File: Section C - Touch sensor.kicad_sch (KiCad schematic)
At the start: 5 parts, among them U2 AT42QT1012-T

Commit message: touch pad library creation
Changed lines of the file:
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@@
 	(rectangle
 		(start 60.96 48.26)
-		(end 229.87 148.59)
+		(end 185.42 148.59)
 		(stroke
 			(width 1)
@@
 	(text_box "DESIGN NOTE:\nblabla"
 		(exclude_from_sim no)
-		(at 127 129.54 0)
+		(at 119.38 124.46 0)
 		(size 21.59 15.24)
 		(margins 1.3525 1.3525 1.3525 1.3525)
@@
 	(text_box "LAYOUT NOTE:\nblabla"
 		(exclude_from_sim no)
-		(at 180.34 63.5 0)
+		(at 91.44 124.46 0)
 		(size 26.67 15.24)
 		(margins 1.4525 1.4525 1.4525 1.4525)
@@
 		(exclude_from_sim no)
 		(at 160.02 111.76 0)
-		(size 21.59 11.43)
+		(size 20.32 11.43)
 		(margins 1.3525 1.3525 1.3525 1.3525)
 		(stroke

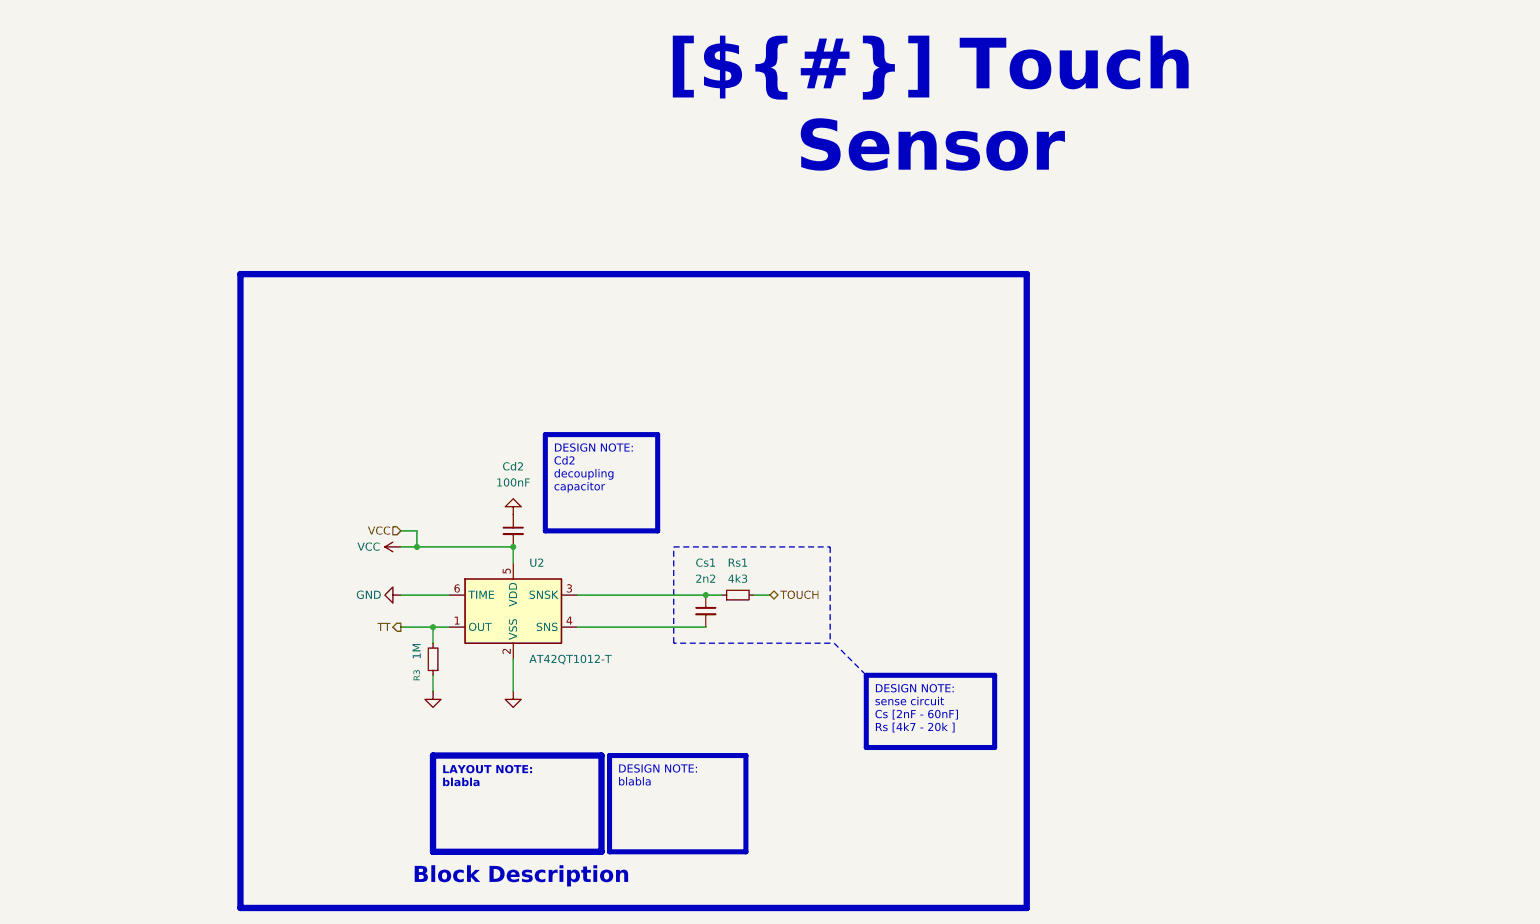
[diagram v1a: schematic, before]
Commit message: [sch] update touch sensor section
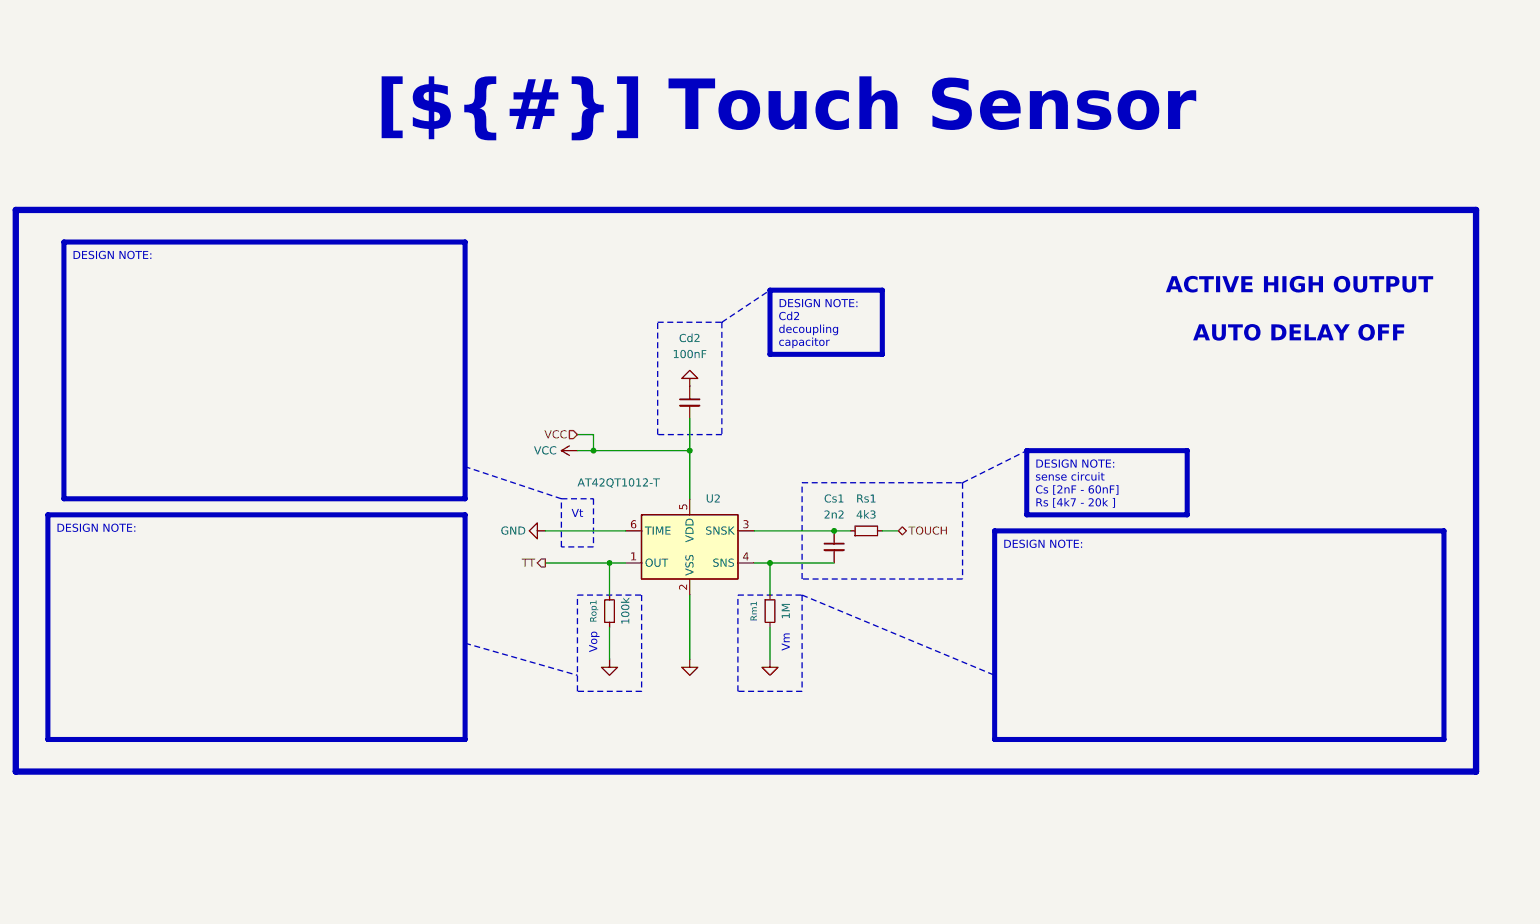
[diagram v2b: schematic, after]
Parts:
- added Rm1: 1M, Resistor_SMD:R_0805_2012Metric, symbol Device:R_Small
- Rop1: renamed from R3; value 1M -> 100k
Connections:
- net GND: now also Rm1.2
- net at Cs1.2, U2.4 (SNS): now also Rm1.1
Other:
- note added: "Vm"
- note added: "Vop"
- note added: "Vt"
- moved on the sheet: Cd2, Cs1, Rop1, Rs1, U2

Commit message: [CFG] Configuration update, added bom information fields
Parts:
- U2: BOM_INFO (none) -> TME have; BOM_STATUS (none) -> OK

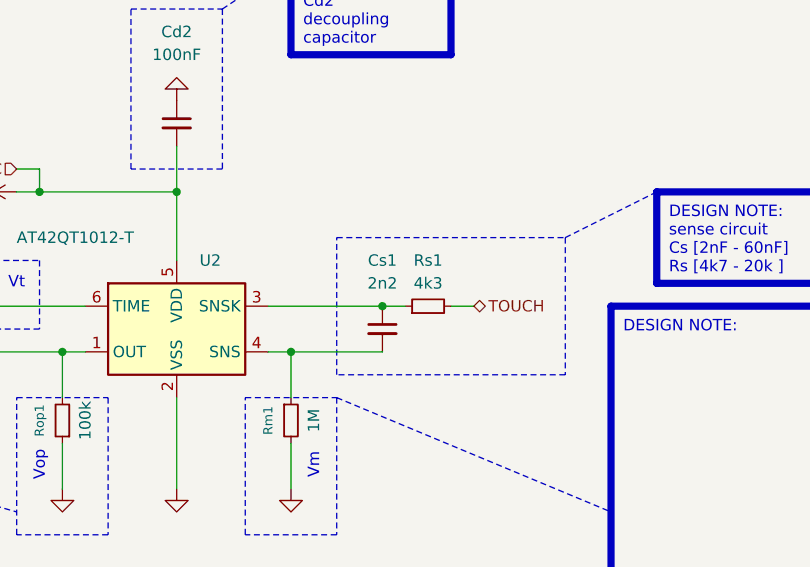
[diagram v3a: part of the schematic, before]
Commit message: bom update, qr-code added
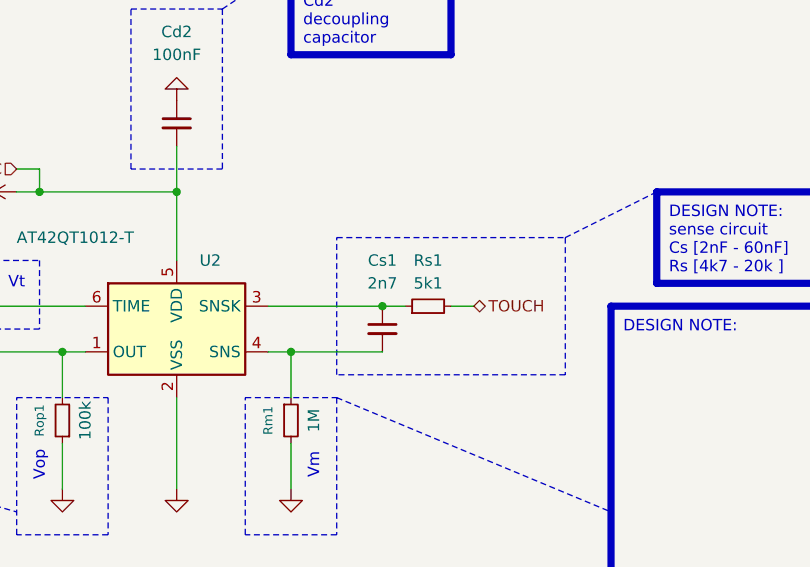
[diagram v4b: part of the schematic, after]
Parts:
- Cd2: BOM_INFO (none) -> AIDATEK A0; BOM_STATUS (none) -> OK
- Cs1: value 2n2 -> 2n7; BOM_INFO (none) -> TME BOX; BOM_STATUS (none) -> OK
- Rm1, Rop1: BOM_INFO (none) -> TME BOX; BOM_STATUS (none) -> OK
- Rs1: value 4k3 -> 5k1; BOM_INFO (none) -> TME BOX 25.06.2025; BOM_STATUS (none) -> OK
- U2: BOM_INFO TME have -> TME BOX
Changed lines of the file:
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@@
 			)
 		)
-		(property "BOM_INFO" "TME have"
+		(property "BOM_INFO" "TME BOX"
 			(at 132.08 91.44 0)
 			(effects
@@
 			)
 		)
-		(property "Value" "4k3"
+		(property "Value" "5k1"
 			(at 160.02 86.36 90)
 			(effects
@@
 			)
 		)
-		(property "BOM_INFO" ""
+		(property "BOM_INFO" "TME BOX 25.06.2025"
 			(at 160.02 88.9 90)
 			(effects
@@
 			)
 		)
-		(property "BOM_STATUS" ""
+		(property "BOM_STATUS" "OK"
 			(at 160.02 88.9 90)
 			(effects
@@
 			)
 		)
-		(property "BOM_INFO" ""
+		(property "BOM_INFO" "TME BOX "
 			(at 119.38 101.6 90)
 			(effects
@@
 			)
 		)
-		(property "BOM_STATUS" ""
+		(property "BOM_STATUS" "OK"
 			(at 119.38 101.6 90)
 			(effects
@@
 			)
 		)
-		(property "BOM_INFO" ""
+		(property "BOM_INFO" "TME BOX"
 			(at 144.78 101.6 90)
 			(effects
@@
 			)
 		)
-		(property "BOM_STATUS" ""
+		(property "BOM_STATUS" "OK"
 			(at 144.78 101.6 90)
 			(effects
@@
 			)
 		)
-		(property "BOM_INFO" ""
-			(at 132.08 68.58 0)
-			(effects
-				(font
-					(size 1.27 1.27)
-				)
-				(hide yes)
-			)
-		)
-		(property "BOM_STATUS" ""
+		(property "BOM_INFO" "AIDATEK A0"
+			(at 132.08 68.58 0)
+			(effects
+				(font
+					(size 1.27 1.27)
+				)
+				(hide yes)
+			)
+		)
+		(property "BOM_STATUS" "OK"
 			(at 132.08 68.58 0)
 			(effects
@@
 			)
 		)
-		(property "Value" "2n2"
+		(property "Value" "2n7"
 			(at 154.94 86.36 0)
 			(effects
@@
 			)
 		)
-		(property "BOM_INFO" ""
+		(property "BOM_INFO" "TME BOX"
 			(at 154.94 91.44 0)
 			(effects
@@
 			)
 		)
-		(property "BOM_STATUS" ""
+		(property "BOM_STATUS" "OK"
 			(at 154.94 91.44 0)
 			(effects

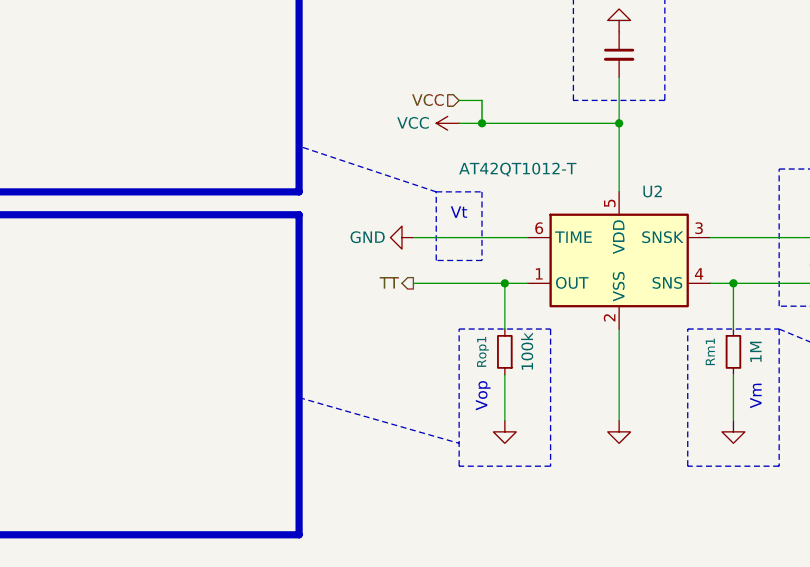
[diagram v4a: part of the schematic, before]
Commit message: [sch] added R3 to prevent high current drain from cap touch chip
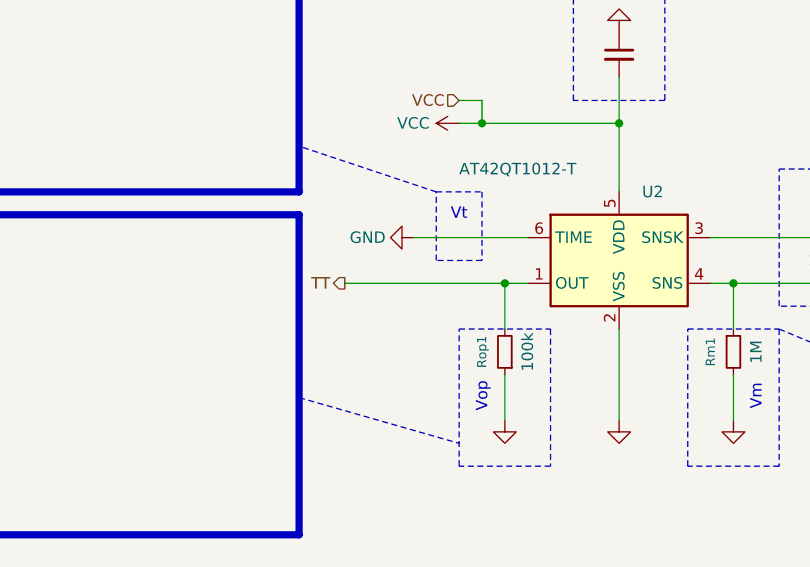
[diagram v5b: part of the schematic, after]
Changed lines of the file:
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@@
 	(wire
 		(pts
-			(xy 109.22 93.98) (xy 119.38 93.98)
+			(xy 101.6 93.98) (xy 119.38 93.98)
 		)
 		(stroke
@@
 	(hierarchical_label "TT"
 		(shape output)
-		(at 109.22 93.98 180)
+		(at 101.6 93.98 180)
 		(effects
 			(font

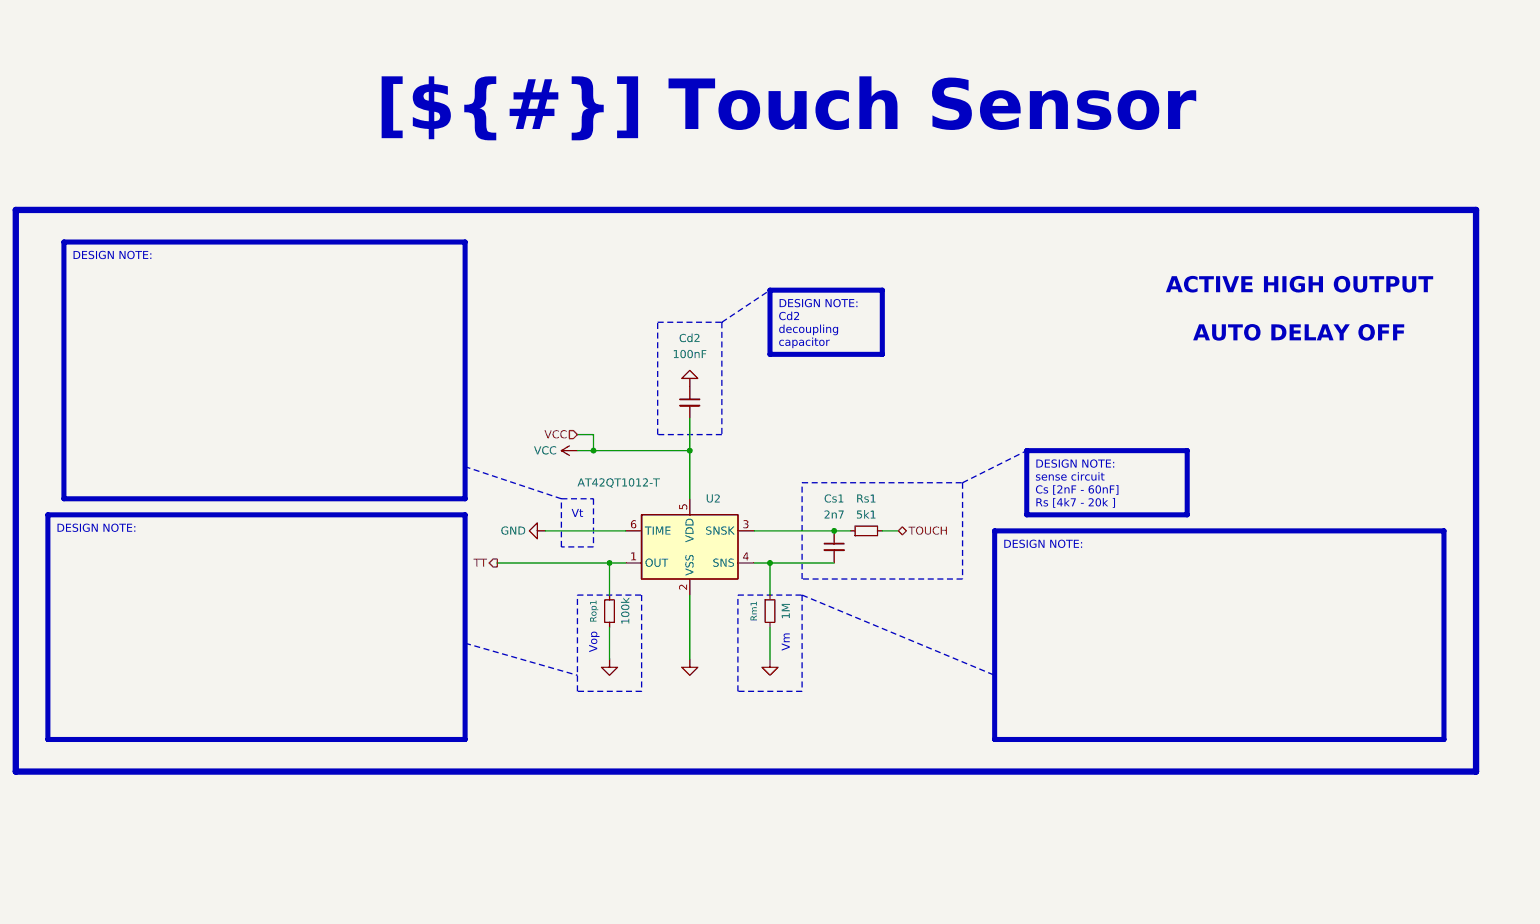
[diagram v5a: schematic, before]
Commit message: documentation update / block diagram
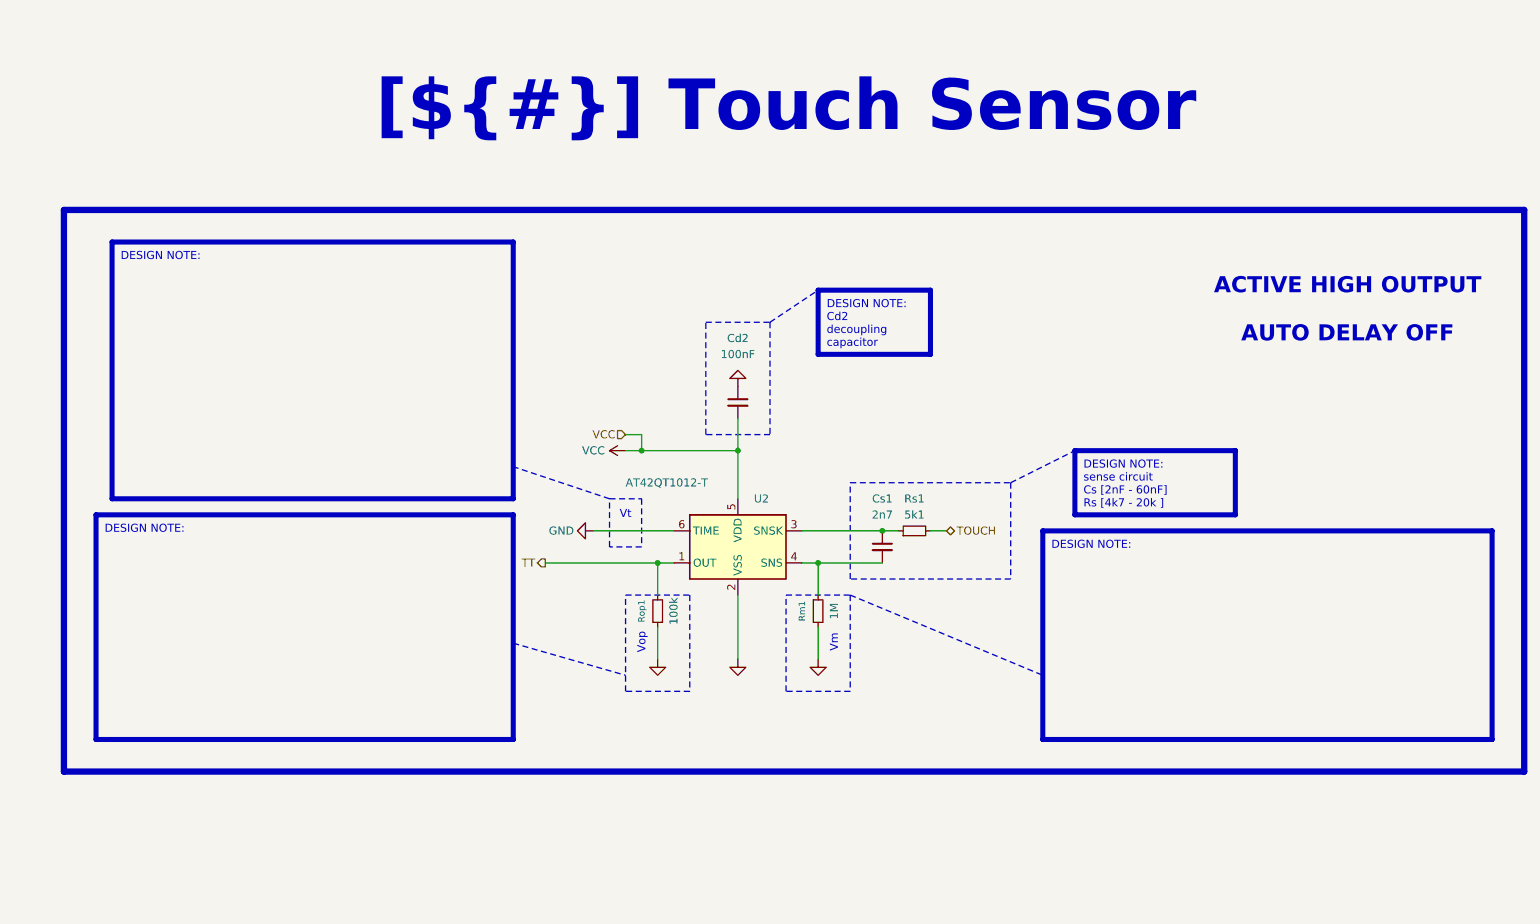
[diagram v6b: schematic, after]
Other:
- moved on the sheet: Cd2, Cs1, Rm1, Rop1, Rs1, U2
